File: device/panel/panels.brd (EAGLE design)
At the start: 132.9 x 72.5 mm, 0 parts

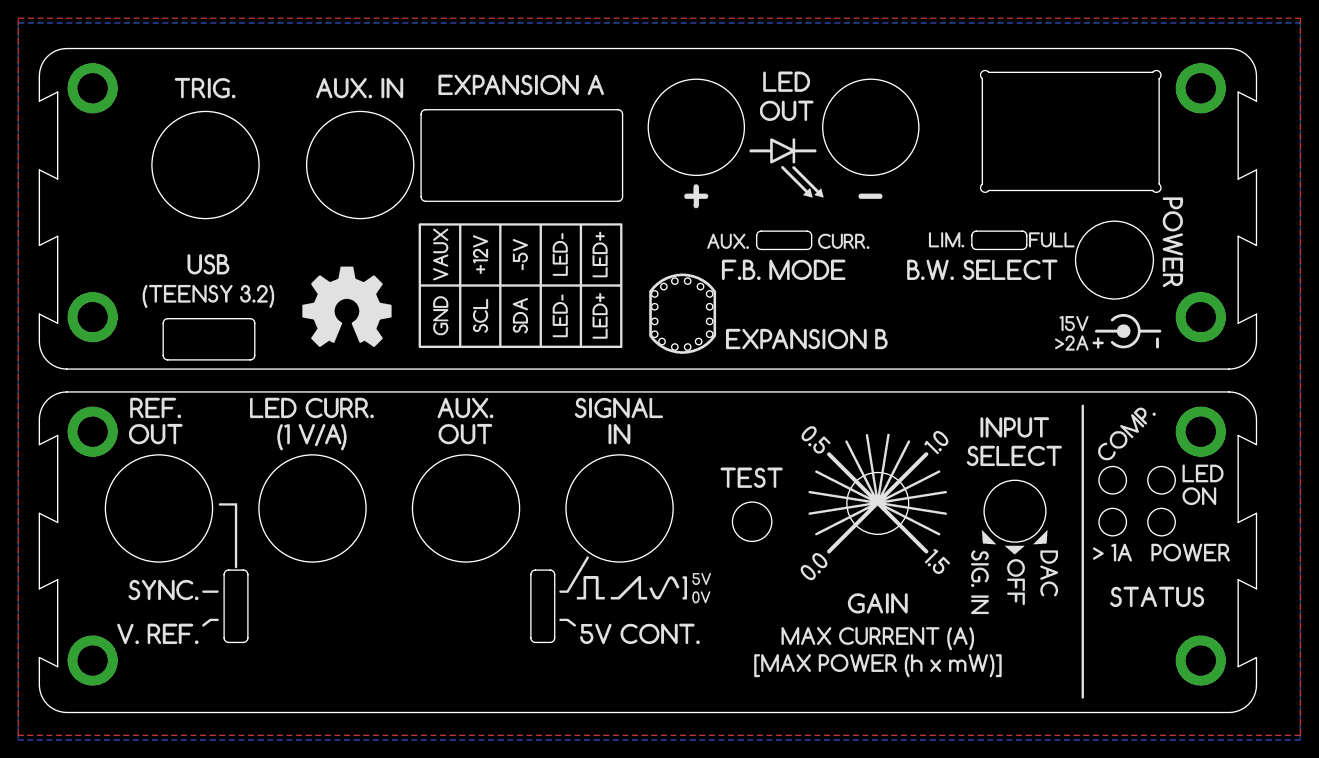
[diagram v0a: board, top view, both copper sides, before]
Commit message: More pre-production fixes for Filipe.
- Better cutouts on Exapansion B in panel
- Panel alignment
- Schematic fixes (remove teensy cut trace/diode requirement)
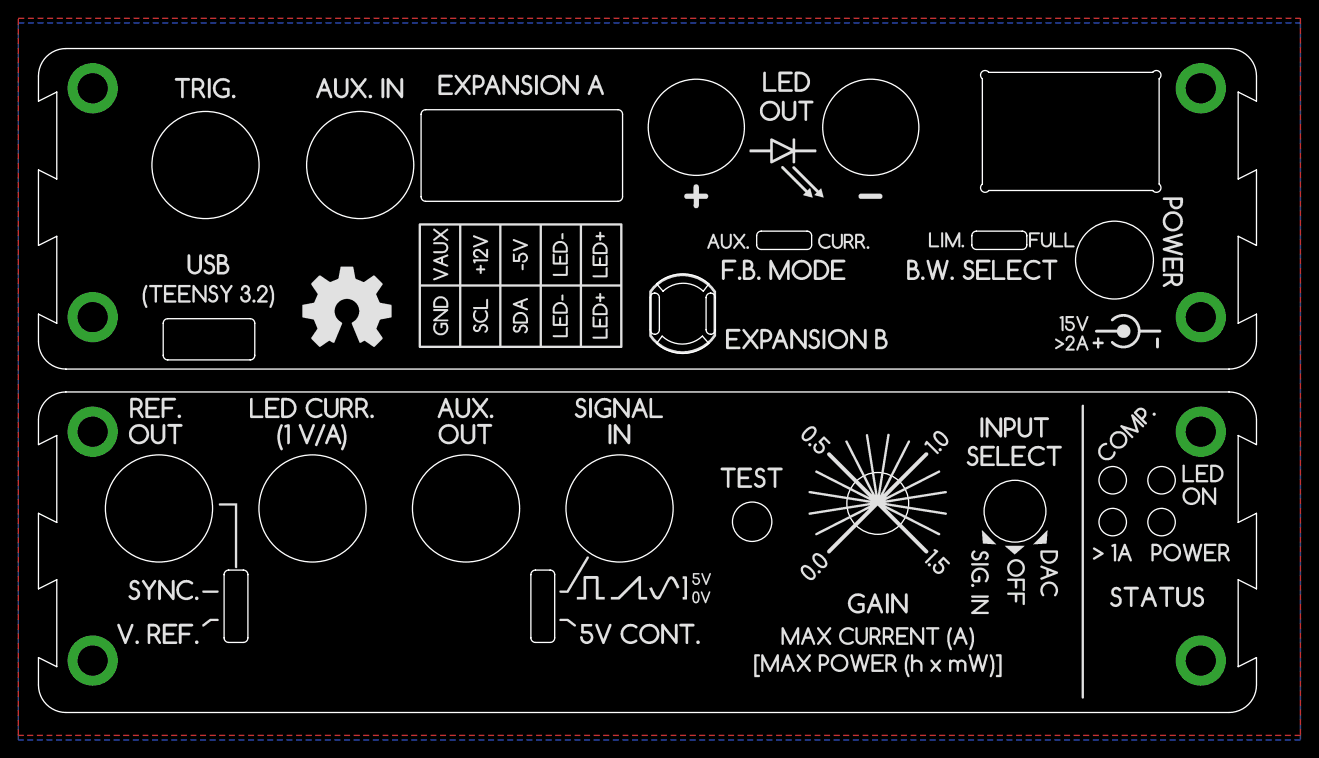
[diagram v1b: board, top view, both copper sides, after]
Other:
- board size 132.9 x 72.5 mm -> 133 x 72.5 mm
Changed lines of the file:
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@@
 <?xml version="1.0" encoding="utf-8"?>
 <!DOCTYPE eagle SYSTEM "eagle.dtd">
-<eagle version="6.5.0">
+<eagle version="6.6.0">
 <drawing>
 <settings>
@@
 <setting verticaltext="up"/>
 </settings>
-<grid distance="3" unitdist="mm" unit="mm" style="lines" multiple="1" display="yes" altdistance="0.025" altunitdist="inch" altunit="inch"/>
+<grid distance="0.1" unitdist="mm" unit="mm" style="lines" multiple="1" display="yes" altdistance="0.025" altunitdist="inch" altunit="inch"/>
 <layers>
 <layer number="1" name="Top" color="4" fill="1" visible="yes" active="yes"/>
@@
 <layer number="42" name="bRestrict" color="1" fill="10" visible="no" active="yes"/>
 <layer number="43" name="vRestrict" color="2" fill="10" visible="no" active="yes"/>
-<layer number="44" name="Drills" color="7" fill="1" visible="no" active="yes"/>
-<layer number="45" name="Holes" color="7" fill="1" visible="no" active="yes"/>
+<layer number="44" name="Drills" color="7" fill="1" visible="yes" active="yes"/>
+<layer number="45" name="Holes" color="7" fill="1" visible="yes" active="yes"/>
 <layer number="46" name="Milling" color="3" fill="1" visible="no" active="yes"/>
 <layer number="47" name="Measures" color="7" fill="1" visible="no" active="yes"/>
@@
 <board>
 <plain>
-<wire x1="0.1" y1="32" x2="0.1" y2="29.25" width="0" layer="20"/>
-<wire x1="0.1" y1="21.75" x2="0.1" y2="13.5" width="0" layer="20"/>
-<wire x1="0.1" y1="6" x2="0.1" y2="3" width="0" layer="20"/>
-<wire x1="0.1" y1="3" x2="3.1" y2="0" width="0" layer="20" curve="90"/>
-<wire x1="3.1" y1="0" x2="130" y2="0" width="0" layer="20"/>
+<wire x1="0" y1="32" x2="0" y2="29.25" width="0" layer="20"/>
+<wire x1="0" y1="21.75" x2="0" y2="13.5" width="0" layer="20"/>
+<wire x1="0" y1="6" x2="0" y2="3" width="0" layer="20"/>
+<wire x1="0" y1="3" x2="3" y2="0" width="0" layer="20" curve="90"/>
+<wire x1="3" y1="0" x2="130" y2="0" width="0" layer="20"/>
 <wire x1="130" y1="0" x2="133" y2="3" width="0" layer="20" curve="90"/>
 <wire x1="133" y1="32" x2="130" y2="35" width="0" layer="20" curve="90"/>
-<wire x1="130" y1="35" x2="3.1" y2="35" width="0" layer="20"/>
-<wire x1="3.1" y1="35" x2="0.1" y2="32" width="0" layer="20" curve="90"/>
-<wire x1="2.1" y1="14.5" x2="2.1" y2="5" width="0" layer="20"/>
-<wire x1="2.1" y1="30.25" x2="2.1" y2="20.75" width="0" layer="20"/>
-<wire x1="2.1" y1="30.25" x2="0.1" y2="29.25" width="0" layer="20"/>
-<wire x1="2.1" y1="20.75" x2="0.1" y2="21.75" width="0" layer="20"/>
-<wire x1="2.1" y1="14.5" x2="0.1" y2="13.5" width="0" layer="20"/>
-<wire x1="2.1" y1="5" x2="0.1" y2="6" width="0" layer="20"/>
+<wire x1="130" y1="35" x2="3" y2="35" width="0" layer="20"/>
+<wire x1="3" y1="35" x2="0" y2="32" width="0" layer="20" curve="90"/>
+<wire x1="2" y1="14.5" x2="2" y2="5" width="0" layer="20"/>
+<wire x1="2" y1="30.25" x2="2" y2="20.75" width="0" layer="20"/>
+<wire x1="2" y1="30.25" x2="0" y2="29.25" width="0" layer="20"/>
+<wire x1="2" y1="20.75" x2="0" y2="21.75" width="0" layer="20"/>
+<wire x1="2" y1="14.5" x2="0" y2="13.5" width="0" layer="20"/>
+<wire x1="2" y1="5" x2="0" y2="6" width="0" layer="20"/>
 <wire x1="131" y1="14.5" x2="131" y2="5" width="0" layer="20"/>
 <wire x1="131" y1="30.25" x2="131" y2="20.75" width="0" layer="20"/>
@@
 <wire x1="55.87" y1="15.55" x2="54.27" y2="15.55" width="0" layer="20"/>
 <wire x1="54.27" y1="15.55" x2="53.77" y2="15.05" width="0" layer="20" curve="90"/>
-<wire x1="0.1" y1="69.5" x2="0.1" y2="66.75" width="0" layer="20"/>
-<wire x1="0.1" y1="59.25" x2="0.1" y2="51" width="0" layer="20"/>
-<wire x1="0.1" y1="43.5" x2="0.1" y2="40.5" width="0" layer="20"/>
-<wire x1="0.1" y1="40.5" x2="3.1" y2="37.5" width="0" layer="20" curve="90"/>
-<wire x1="3.1" y1="37.5" x2="130" y2="37.5" width="0" layer="20"/>
+<wire x1="0" y1="69.5" x2="0" y2="66.75" width="0" layer="20"/>
+<wire x1="0" y1="59.25" x2="0" y2="51" width="0" layer="20"/>
+<wire x1="0" y1="43.5" x2="0" y2="40.5" width="0" layer="20"/>
+<wire x1="0" y1="40.5" x2="3" y2="37.5" width="0" layer="20" curve="90"/>
+<wire x1="3" y1="37.5" x2="130" y2="37.5" width="0" layer="20"/>
 <wire x1="130" y1="37.5" x2="133" y2="40.5" width="0" layer="20" curve="90"/>
 <wire x1="133" y1="69.5" x2="130" y2="72.5" width="0" layer="20" curve="90"/>
-<wire x1="130" y1="72.5" x2="3.1" y2="72.5" width="0" layer="20"/>
-<wire x1="3.1" y1="72.5" x2="0.1" y2="69.5" width="0" layer="20" curve="90"/>
-<wire x1="2.1" y1="52" x2="2.1" y2="42.5" width="0" layer="20"/>
-<wire x1="2.1" y1="67.75" x2="2.1" y2="58.25" width="0" layer="20"/>
-<wire x1="2.1" y1="67.75" x2="0.1" y2="66.75" width="0" layer="20"/>
-<wire x1="2.1" y1="58.25" x2="0.1" y2="59.25" width="0" layer="20"/>
-<wire x1="2.1" y1="52" x2="0.1" y2="51" width="0" layer="20"/>
-<wire x1="2.1" y1="42.5" x2="0.1" y2="43.5" width="0" layer="20"/>
+<wire x1="130" y1="72.5" x2="3" y2="72.5" width="0" layer="20"/>
+<wire x1="3" y1="72.5" x2="0" y2="69.5" width="0" layer="20" curve="90"/>
+<wire x1="2" y1="52" x2="2" y2="42.5" width="0" layer="20"/>
+<wire x1="2" y1="67.75" x2="2" y2="58.25" width="0" layer="20"/>
+<wire x1="2" y1="67.75" x2="0" y2="66.75" width="0" layer="20"/>
+<wire x1="2" y1="58.25" x2="0" y2="59.25" width="0" layer="20"/>
+<wire x1="2" y1="52" x2="0" y2="51" width="0" layer="20"/>
+<wire x1="2" y1="42.5" x2="0" y2="43.5" width="0" layer="20"/>
 <wire x1="131" y1="52" x2="131" y2="42.5" width="0" layer="20"/>
 <wire x1="131" y1="67.75" x2="131" y2="58.25" width="0" layer="20"/>
@@
 <wire x1="78.425" y1="51.06" x2="78.425" y2="52.06" width="0" layer="20"/>
 <wire x1="78.425" y1="52.06" x2="78.925" y2="52.56" width="0" layer="20" curve="-90"/>
-<hole x="67.2904" y="45.7056" drill="0.7"/>
-<hole x="67.2904" y="41.3056" drill="0.7"/>
-<hole x="67.2904" y="44.3056" drill="0.7"/>
-<hole x="67.2904" y="42.7056" drill="0.7"/>
-<hole x="73.2904" y="45.7056" drill="0.7"/>
-<hole x="73.2904" y="41.3056" drill="0.7"/>
-<hole x="73.2904" y="44.3056" drill="0.7"/>
-<hole x="73.2904" y="42.7056" drill="0.7"/>
-<hole x="68.2904" y="46.5056" drill="0.7"/>
-<hole x="69.4904" y="47.1056" drill="0.7"/>
-<hole x="70.8904" y="47.1056" drill="0.7"/>
-<hole x="72.2904" y="46.5056" drill="0.7"/>
-<hole x="72.0904" y="40.5056" drill="0.7"/>
-<hole x="70.8904" y="39.9056" drill="0.7"/>
-<hole x="69.4904" y="39.9056" drill="0.7"/>
-<hole x="68.0904" y="40.5056" drill="0.7"/>
 <rectangle x1="22.8473" y1="0.1905" x2="53.5559" y2="0.2159" layer="29"/>
 <rectangle x1="22.8727" y1="0.2159" x2="53.5559" y2="0.2413" layer="29"/>
@@
 <rectangle x1="38.148259375" y1="69.262753125" x2="38.211759375" y2="69.294246875" layer="21"/>
 <rectangle x1="39.639240625" y1="69.262753125" x2="39.672259375" y2="69.294246875" layer="21"/>
+<wire x1="67.8" y1="45.3" x2="67.8" y2="41.8" width="0" layer="20"/>
+<wire x1="67.8" y1="41.8" x2="67.3" y2="41.3" width="0" layer="20" curve="-90"/>
+<wire x1="67.3" y1="41.3" x2="66.8" y2="41.8" width="0" layer="20" curve="-90"/>
+<wire x1="66.8" y1="41.8" x2="66.8" y2="45.3" width="0" layer="20"/>
+<wire x1="66.8" y1="45.3" x2="67.3" y2="45.8" width="0" layer="20" curve="-90"/>
+<wire x1="67.3" y1="45.8" x2="67.8" y2="45.3" width="0" layer="20" curve="-90"/>
+<wire x1="73.9" y1="45.3" x2="73.9" y2="41.8" width="0" layer="20"/>
+<wire x1="73.9" y1="41.8" x2="73.4" y2="41.3" width="0" layer="20" curve="-90"/>
+<wire x1="73.4" y1="41.3" x2="72.9" y2="41.8" width="0" layer="20" curve="-90"/>
+<wire x1="72.9" y1="41.8" x2="72.9" y2="45.3" width="0" layer="20"/>
+<wire x1="72.9" y1="45.3" x2="73.4" y2="45.8" width="0" layer="20" curve="-90"/>
+<wire x1="73.4" y1="45.8" x2="73.9" y2="45.3" width="0" layer="20" curve="-90"/>
+<wire x1="67.5" y1="46.8" x2="73.2" y2="46.8" width="0" layer="20" curve="-84.27519"/>
+<wire x1="68.2" y1="46" x2="72.6" y2="46" width="0" layer="20" curve="-86.528591"/>
+<wire x1="67.5" y1="46.8" x2="68.2" y2="46" width="0" layer="20"/>
+<wire x1="72.6" y1="46" x2="73.2" y2="46.8" width="0" layer="20"/>
+<wire x1="73.2" y1="40.3" x2="67.5" y2="40.3" width="0" layer="20" curve="-84.27519"/>
+<wire x1="72.5" y1="41.1" x2="68.1" y2="41.1" width="0" layer="20" curve="-86.528591"/>
+<wire x1="73.2" y1="40.3" x2="72.5" y2="41.1" width="0" layer="20"/>
+<wire x1="68.1" y1="41.1" x2="67.5" y2="40.3" width="0" layer="20"/>
 </plain>
 <attributes>
